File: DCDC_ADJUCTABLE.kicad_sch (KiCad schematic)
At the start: 36 parts, among them Q1601 NMOS, Q1602 NMOS, Q1603 NMOS, U1601 TPS62933, U1602 TPS62933, U1603 LM74700, U1604 LM74700

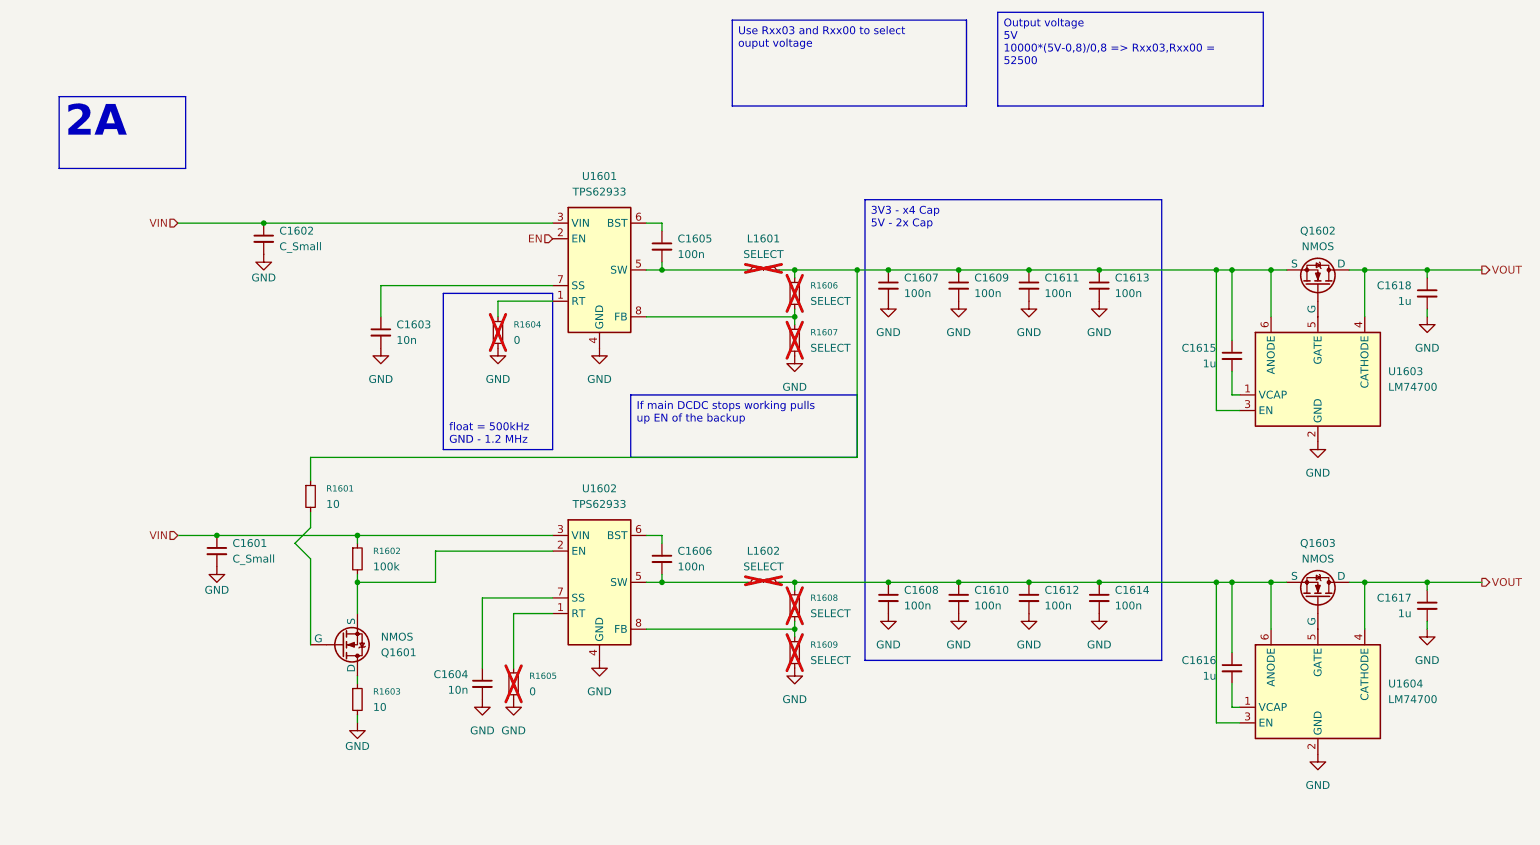
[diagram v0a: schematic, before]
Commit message: deleted unused sheets, added standalone current measure sheet
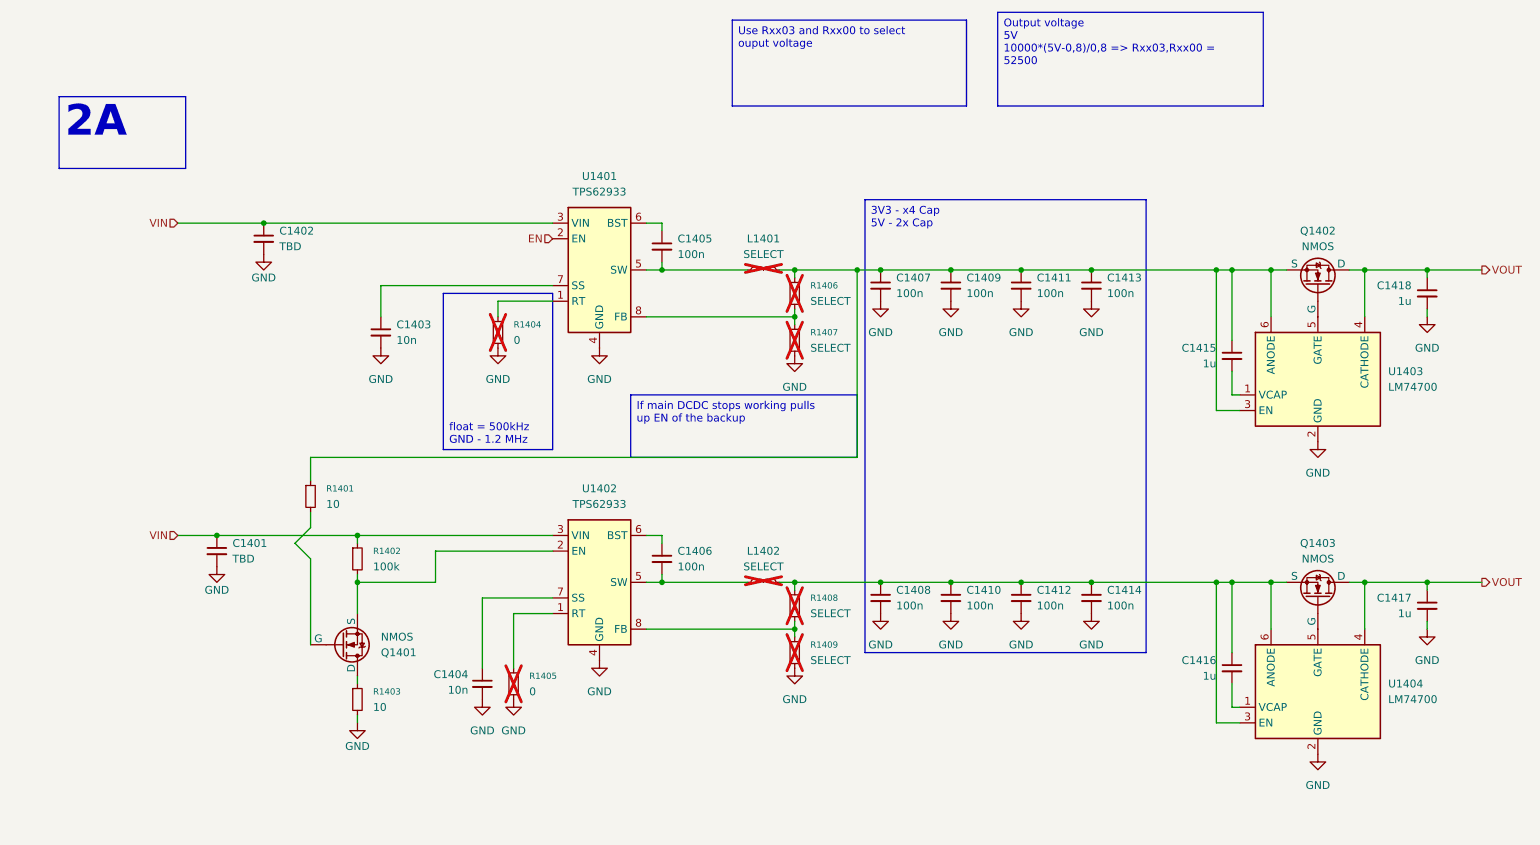
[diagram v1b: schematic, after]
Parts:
- C1401: renamed from C1601; value C_Small -> TBD
- C1402: renamed from C1602; value C_Small -> TBD
- renumbered C1603 to C1403, C1604 to C1404, C1605 to C1405, C1606 to C1406, C1607 to C1407, C1608 to C1408, C1609 to C1409, C1610 to C1410, C1611 to C1411, C1612 to C1412, C1613 to C1413, C1614 to C1414, C1615 to C1415, C1616 to C1416, C1617 to C1417, C1618 to C1418, L1601 to L1401, L1602 to L1402, Q1601 to Q1401, Q1602 to Q1402, Q1603 to Q1403, R1601 to R1401, R1602 to R1402, R1603 to R1403, R1604 to R1404, R1605 to R1405, R1606 to R1406, R1607 to R1407, R1608 to R1408, R1609 to R1409, U1601 to U1401, U1602 to U1402, U1603 to U1403, U1604 to U1404
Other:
- moved on the sheet: C1407, C1408, C1409, C1410, C1411, C1412, C1413, C1414

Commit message: wired channel alerts; added schematic for test pbc
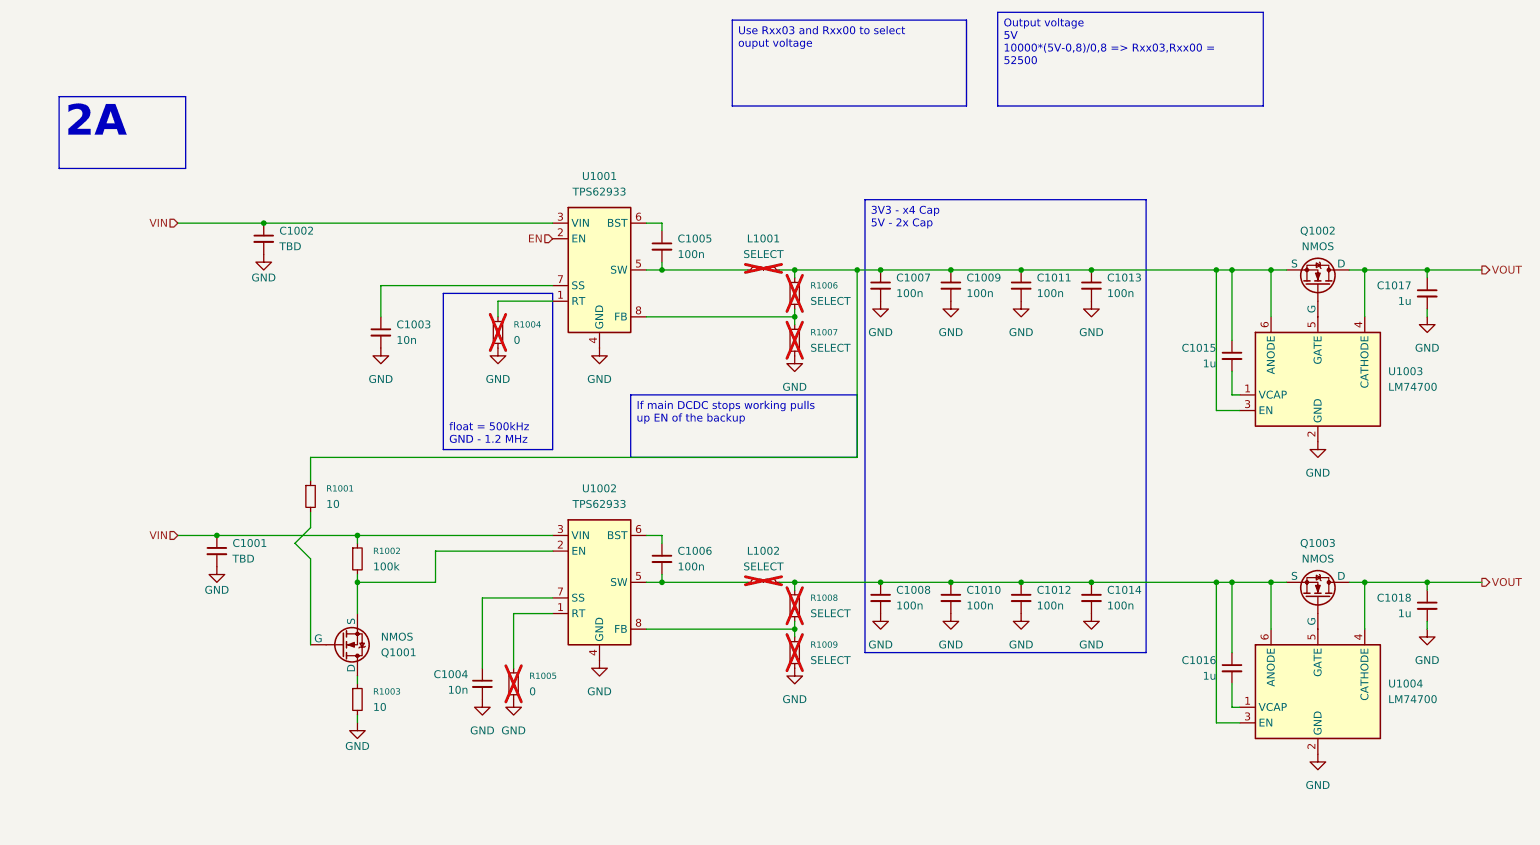
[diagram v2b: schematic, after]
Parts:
- renumbered C1401 to C1001, C1402 to C1002, C1403 to C1003, C1404 to C1004, C1405 to C1005, C1406 to C1006, C1407 to C1007, C1408 to C1008, C1409 to C1009, C1410 to C1010, C1411 to C1011, C1412 to C1012, C1413 to C1013, C1414 to C1014, C1415 to C1015, C1416 to C1016, C1418 to C1017, C1417 to C1018, L1401 to L1001, L1402 to L1002, Q1401 to Q1001, Q1402 to Q1002, Q1403 to Q1003, R1401 to R1001, R1402 to R1002, R1403 to R1003, R1404 to R1004, R1405 to R1005, R1406 to R1006, R1407 to R1007, R1408 to R1008, R1409 to R1009, U1401 to U1001, U1402 to U1002, U1403 to U1003, U1404 to U1004

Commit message: reduced number of DCDC converter for PV panels; updated test pcb
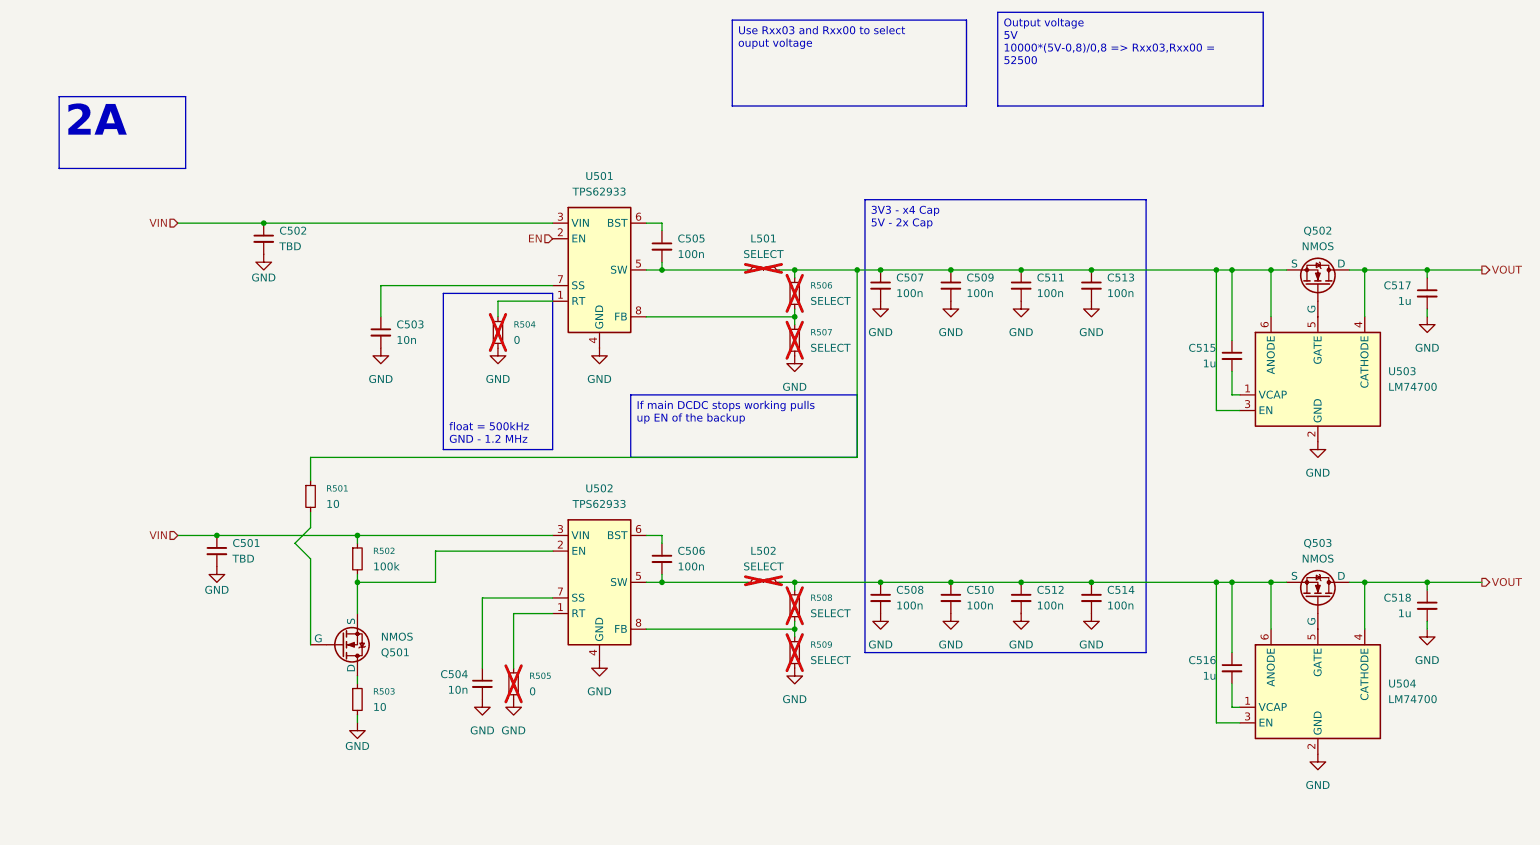
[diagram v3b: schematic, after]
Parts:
- Q502: renamed from Q1002; footprint Package_TO_SOT_SMD:SOT-23-6 -> Outlines:NVTFS5116PLTWG
- Q503: renamed from Q1003; footprint Package_TO_SOT_SMD:SOT-23-6 -> Outlines:NVTFS5116PLTWG
- renumbered C1001 to C501, C1002 to C502, C1003 to C503, C1004 to C504, C1005 to C505, C1006 to C506, C1007 to C507, C1008 to C508, C1009 to C509, C1010 to C510, C1011 to C511, C1012 to C512, C1013 to C513, C1014 to C514, C1015 to C515, C1016 to C516, C1017 to C517, C1018 to C518, L1001 to L501, L1002 to L502, Q1001 to Q501, R1001 to R501, R1002 to R502, R1003 to R503, R1004 to R504, R1005 to R505, R1006 to R506, R1007 to R507, R1008 to R508, R1009 to R509, U1001 to U501, U1002 to U502, U1003 to U503, U1004 to U504

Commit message: added missing heater connectors
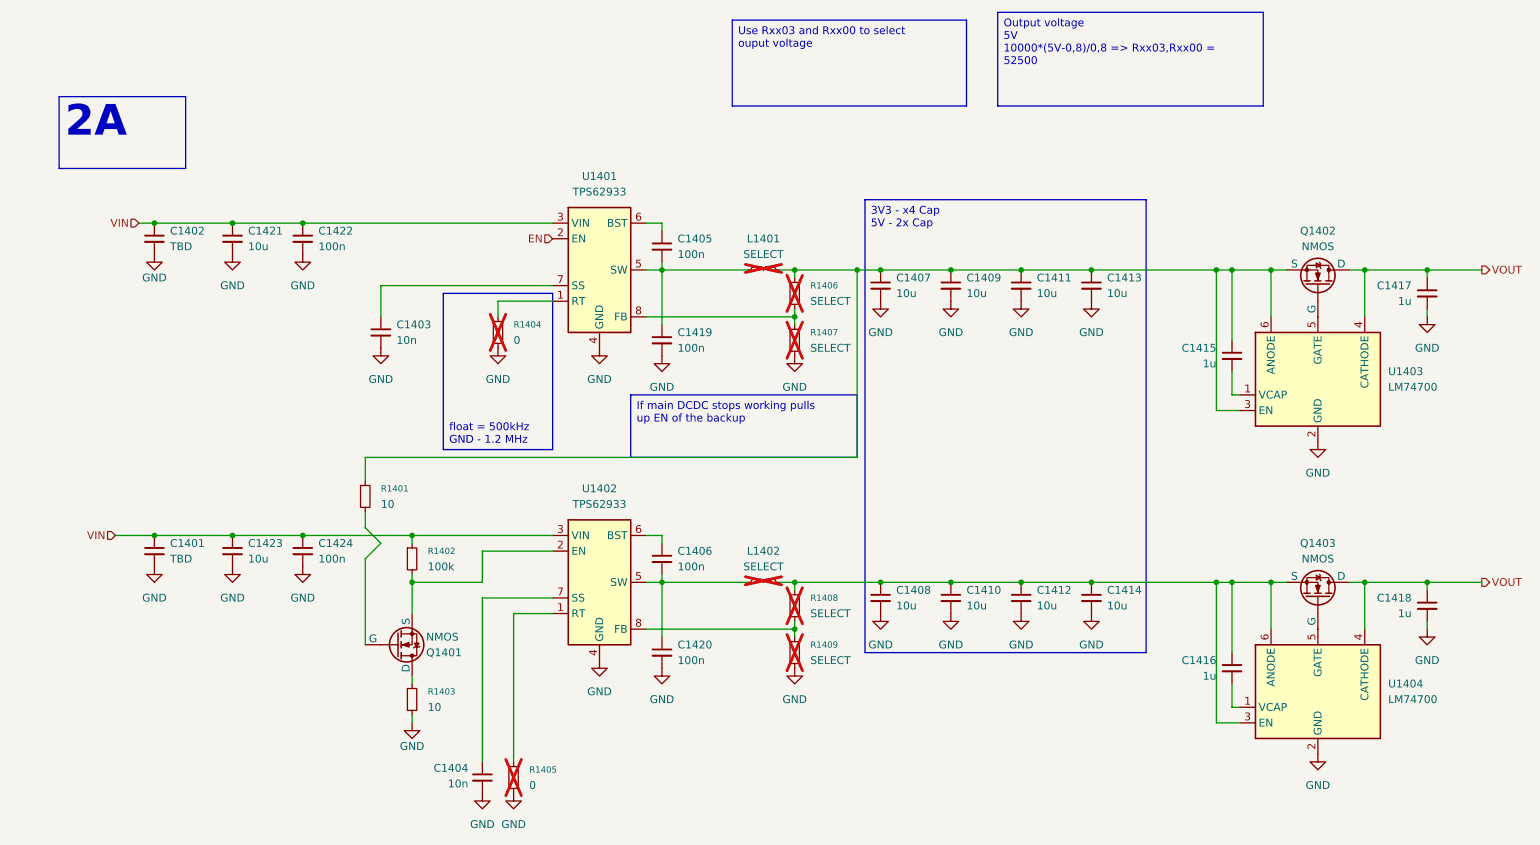
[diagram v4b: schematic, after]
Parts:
- added C1419, C1420, C1422, C1424: 100n, Capacitor_SMD:C_0603_1608Metric_Pad1.08x0.95mm_HandSolder, symbol Device:C_Small
- added C1421, C1423: 10u, Capacitor_SMD:C_0603_1608Metric_Pad1.08x0.95mm_HandSolder, symbol Device:C_Small
- C1407: renamed from C507; value 100n -> 10u
- C1408: renamed from C508; value 100n -> 10u
- C1409: renamed from C509; value 100n -> 10u
- C1410: renamed from C510; value 100n -> 10u
- C1411: renamed from C511; value 100n -> 10u
- C1412: renamed from C512; value 100n -> 10u
- C1413: renamed from C513; value 100n -> 10u
- C1414: renamed from C514; value 100n -> 10u
- renumbered C501 to C1401, C502 to C1402, C503 to C1403, C504 to C1404, C505 to C1405, C506 to C1406, C515 to C1415, C516 to C1416, C517 to C1417, C518 to C1418, L501 to L1401, L502 to L1402, Q501 to Q1401, Q502 to Q1402, Q503 to Q1403, R501 to R1401, R502 to R1402, R503 to R1403, R504 to R1404, R505 to R1405, R506 to R1406, R507 to R1407, R508 to R1408, R509 to R1409, U501 to U1401, U502 to U1402, U503 to U1403, U504 to U1404
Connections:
- net GND: now also C1419.2, C1420.2, C1421.2, C1422.2, C1423.2, C1424.2
- net VIN: now also C1421.1, C1422.1, C1423.1, C1424.1
- net at C1406.2, L1402.1, U1402.5 (SW): now also C1420.1
- net at C1405.2, L1401.1, U1401.5 (SW): now also C1419.1
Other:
- moved on the sheet: C1401, C1402, C1404, Q1401, R1401, R1402, R1403, R1405

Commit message: restructurization of the entire project improved
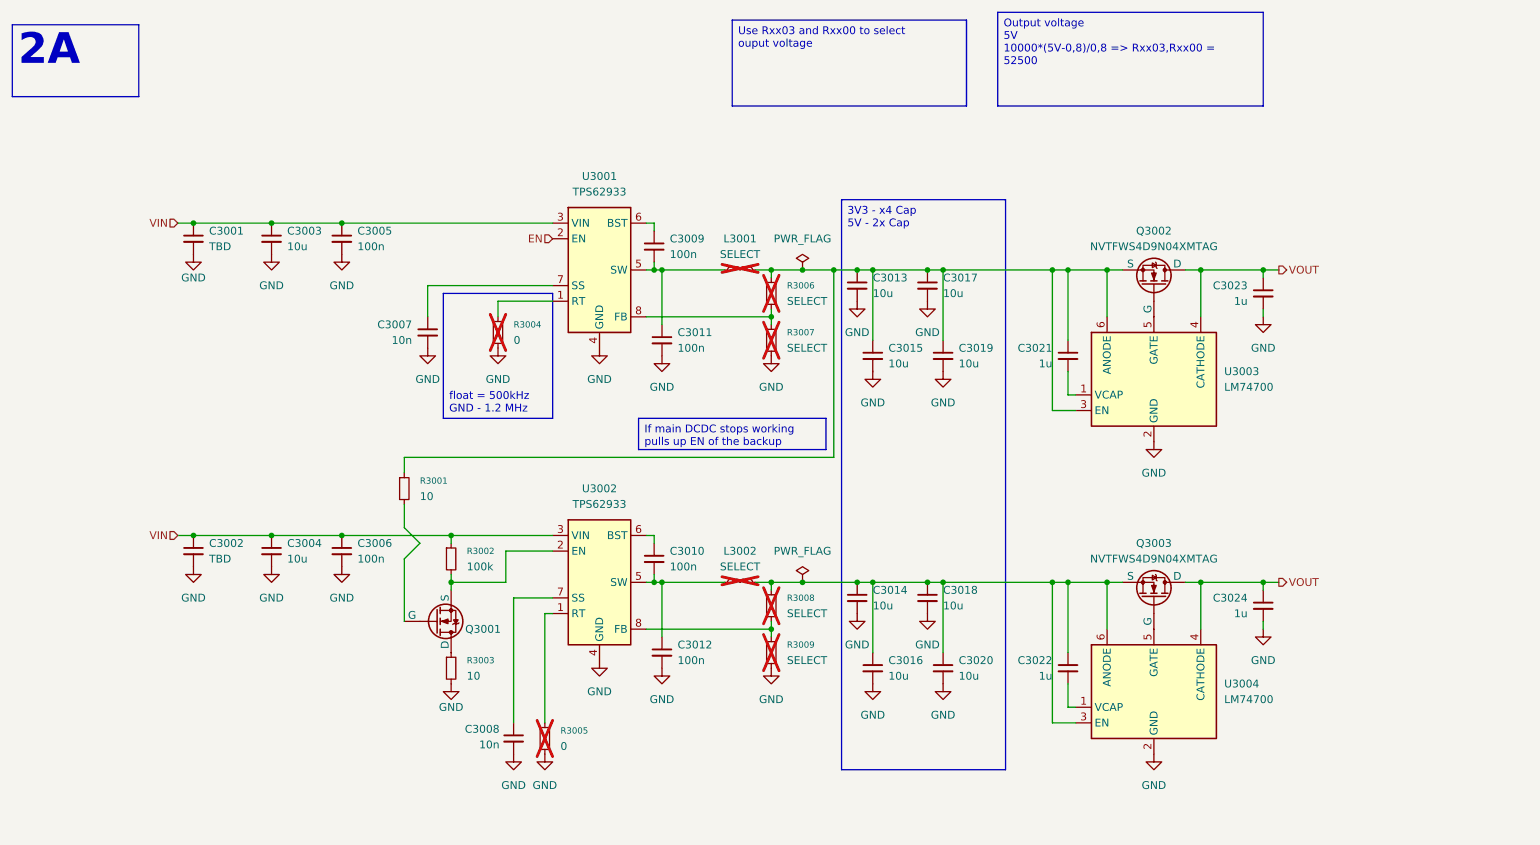
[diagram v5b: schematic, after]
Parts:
- removed C1401, C1402: TBD, Capacitor_SMD:C_0603_1608Metric_Pad1.08x0.95mm_HandSolder, symbol Device:C_Small
- removed C1403, C1404: 10n, Capacitor_SMD:C_0603_1608Metric_Pad1.08x0.95mm_HandSolder, symbol Device:C_Small
- removed C1405, C1406, C1419, C1420, C1422, C1424: 100n, Capacitor_SMD:C_0603_1608Metric_Pad1.08x0.95mm_HandSolder, symbol Device:C_Small
- removed C1407, C1408, C1409, C1410, C1411, C1412, C1413, C1414, C1421, C1423: 10u, Capacitor_SMD:C_0603_1608Metric_Pad1.08x0.95mm_HandSolder, symbol Device:C_Small
- removed C1415, C1416, C1417, C1418: 1u, Capacitor_SMD:C_0603_1608Metric_Pad1.08x0.95mm_HandSolder, symbol Device:C_Small
- removed L1401, L1402: SELECT, Inductor_SMD:L_Taiyo-Yuden_NR-10050_9.8x10.0mm_HandSoldering, symbol Device:L_Small
- removed Q1401: NMOS, Package_TO_SOT_SMD:SOT-23, symbol Simulation_SPICE:NMOS
- removed Q1402, Q1403: NMOS, Outlines:NVTFS5116PLTWG, symbol Simulation_SPICE:NMOS
- removed R1401, R1403: 10, Resistor_SMD:R_0603_1608Metric_Pad0.98x0.95mm_HandSolder, symbol Device:R_Small
- removed R1402: 100k, Resistor_SMD:R_0603_1608Metric_Pad0.98x0.95mm_HandSolder, symbol Device:R_Small
- removed R1404, R1405: 0, Resistor_SMD:R_0603_1608Metric_Pad0.98x0.95mm_HandSolder, symbol Device:R_Small
- removed R1406, R1407, R1408, R1409: SELECT, Resistor_SMD:R_0603_1608Metric_Pad0.98x0.95mm_HandSolder, symbol Device:R_Small
- removed U1401, U1402: TPS62933, Package_TO_SOT_SMD:SOT-583-8, symbol Regulator_Switching:TPS62933
- removed U1403, U1404: LM74700, Package_TO_SOT_SMD:SOT-23-6, symbol Power_Management:LM74700
- added C3001, C3002: TBD, Capacitor_SMD:C_0603_1608Metric_Pad1.08x0.95mm_HandSolder, symbol Device:C_Small
- added C3003, C3004, C3013, C3014, C3015, C3016, C3017, C3018, C3019, C3020: 10u, Capacitor_SMD:C_0603_1608Metric_Pad1.08x0.95mm_HandSolder, symbol Device:C_Small
- added C3005, C3006, C3009, C3010, C3011, C3012: 100n, Capacitor_SMD:C_0603_1608Metric_Pad1.08x0.95mm_HandSolder, symbol Device:C_Small
- added C3007, C3008: 10n, Capacitor_SMD:C_0603_1608Metric_Pad1.08x0.95mm_HandSolder, symbol Device:C_Small
- added C3021, C3022, C3023, C3024: 1u, Capacitor_SMD:C_0603_1608Metric_Pad1.08x0.95mm_HandSolder, symbol Device:C_Small
- added L3001, L3002: SELECT, Inductor_SMD:L_Vishay_IHLP-2525, symbol Device:L_Small
- added Q3001: IRLML5103, Package_TO_SOT_SMD:SOT-23, symbol Simulation_SPICE:NMOS
- added Q3002, Q3003: NVTFWS4D9N04XMTAG, Outlines:NVTFS5116PLTWG, symbol Simulation_SPICE:NMOS
- added R3001, R3003: 10, Resistor_SMD:R_0603_1608Metric_Pad0.98x0.95mm_HandSolder, symbol Device:R_Small
- added R3002: 100k, Resistor_SMD:R_0603_1608Metric_Pad0.98x0.95mm_HandSolder, symbol Device:R_Small
- added R3004, R3005: 0, Resistor_SMD:R_0603_1608Metric_Pad0.98x0.95mm_HandSolder, symbol Device:R_Small
- added R3006, R3007, R3008, R3009: SELECT, Resistor_SMD:R_0603_1608Metric_Pad0.98x0.95mm_HandSolder, symbol Device:R_Small
- added U3001, U3002: TPS62933, Package_TO_SOT_SMD:SOT-583-8, symbol Regulator_Switching:TPS62933
- added U3003, U3004: LM74700, Package_TO_SOT_SMD:SOT-23-6, symbol Power_Management:LM74700
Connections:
- net EN: now also U3001.2 (EN)
- net GND: now also C3001.2, C3002.2, C3003.2, C3004.2, C3005.2, C3006.2, C3007.2, C3008.2, C3011.2, C3012.2, C3013.2, C3014.2, C3015.2, C3016.2, C3017.2, C3018.2, C3019.2, C3020.2, C3023.2, C3024.2, R3003.2, R3004.1, R3005.1, R3007.1, R3009.1, U3001.4 (GND), U3002.4 (GND), U3003.2 (GND), U3004.2 (GND)
- net VIN: now also C3001.1, C3002.1, C3003.1, C3004.1, C3005.1, C3006.1, R3002.1, U3001.3 (VIN), U3002.3 (VIN)
- net VOUT: now also C3023.1, C3024.1, Q3002.1 (D), Q3003.1 (D), U3003.4 (CATHODE), U3004.4 (CATHODE)
- new net: C3014.1, C3016.1, C3018.1, C3020.1, C3022.1, L3002.2, Q3003.3 (S), R3008.2, U3004.3 (EN), U3004.6 (ANODE)
- new net: C3010.2, C3012.1, L3002.1, U3002.5 (SW)
- new net: R3004.2, U3001.1 (RT)
- new net: C3009.2, C3011.1, L3001.1, U3001.5 (SW)
- new net: C3009.1, U3001.6 (BST)
- new net: R3008.1, R3009.2, U3002.8 (FB)
- new net: C3013.1, C3015.1, C3017.1, C3019.1, C3021.1, L3001.2, Q3002.3 (S), R3001.1, R3006.2, U3003.3 (EN), U3003.6 (ANODE)
- new net: C3010.1, U3002.6 (BST)
- new net: Q3001.1 (D), R3003.1
- new net: Q3001.2 (G), R3001.2
- new net: Q3001.3 (S), R3002.2, U3002.2 (EN)
- new net: C3007.1, U3001.7 (SS)
- new net: R3006.1, R3007.2, U3001.8 (FB)
- new net: C3022.2, U3004.1 (VCAP)
- new net: C3021.2, U3003.1 (VCAP)
- new net: R3005.2, U3002.1 (RT)
- new net: C3008.1, U3002.7 (SS)
- new net: Q3002.2 (G), U3003.5 (GATE)
- new net: Q3003.2 (G), U3004.5 (GATE)
